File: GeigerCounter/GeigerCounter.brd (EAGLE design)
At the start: 38.1 x 35.6 mm, 37 parts, among them IC1 OPAMP-DUALU, P1 XF2M-0615-1A

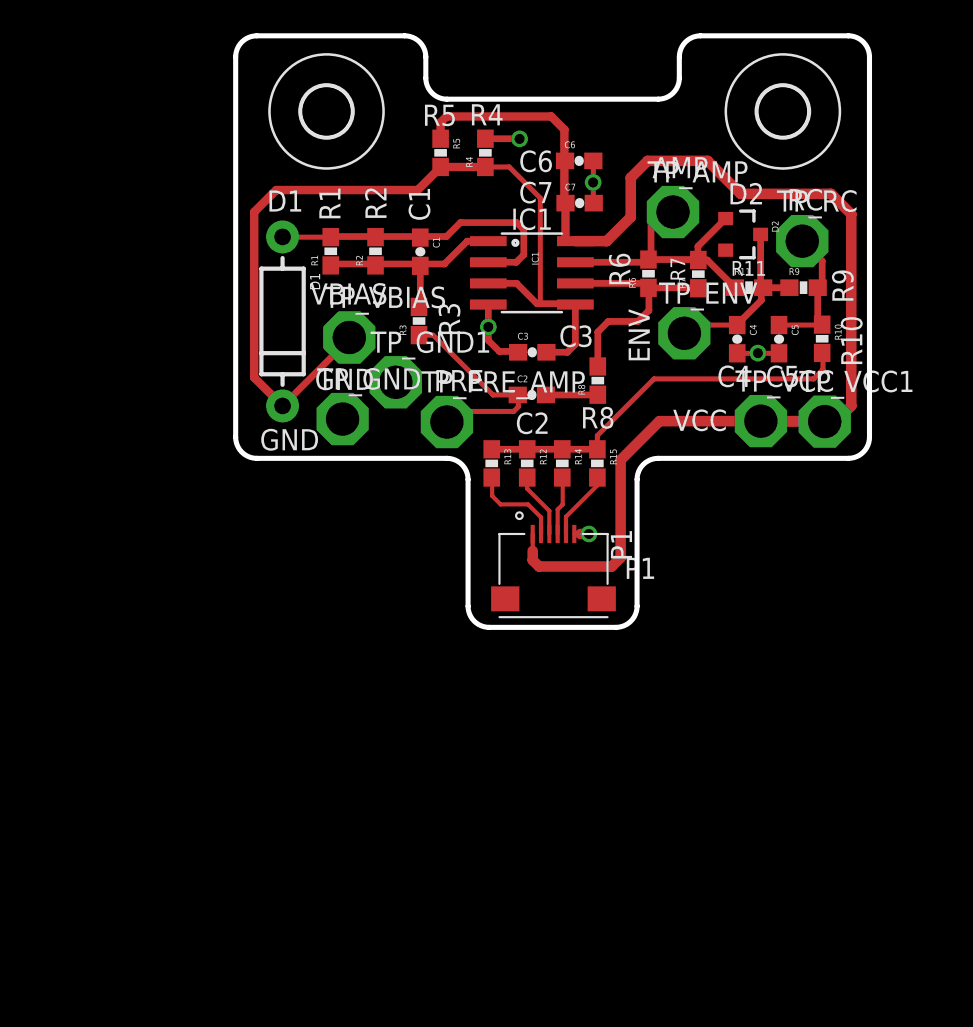
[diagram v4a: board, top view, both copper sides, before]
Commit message: All unrouted nets now routed
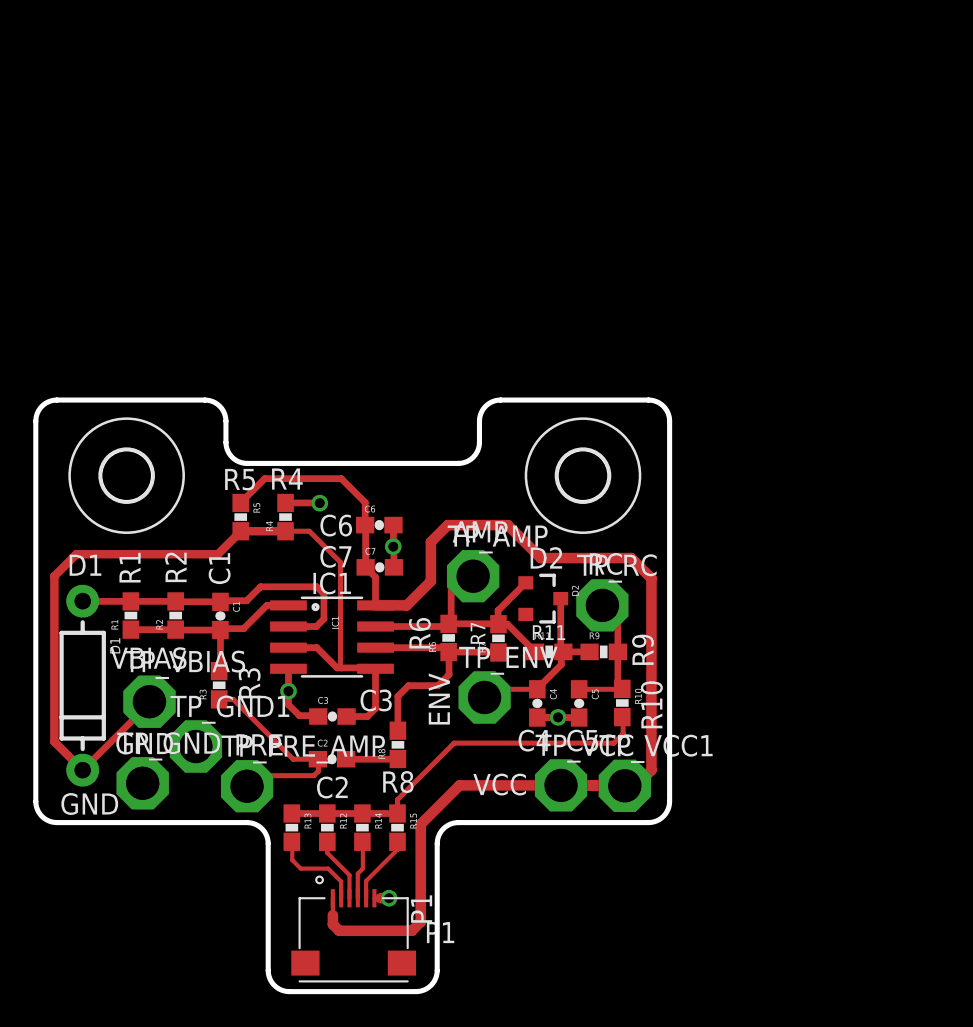
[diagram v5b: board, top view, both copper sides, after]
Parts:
- moved H2 25.0 mm to (36.1, 34.5)
- moved R14 25.0 mm to (22.9, 13.4)
- moved R8 25.0 mm to (25.0, 18.3)
- moved C1 25.0 mm to (14.3, 26.1)
- moved C4 25.0 mm to (33.4, 20.8)
- moved C5 25.0 mm to (35.9, 20.8)
- moved C7 25.0 mm to (23.9, 29.0)
- moved D2 25.0 mm to (33.7, 27.1)
- moved H1 25.0 mm to (8.69, 34.5)
- moved IC1 25.0 mm to (21.0, 24.8)
- moved P1 25.0 mm to (22.4, 6.58)
- moved R12 25.0 mm to (20.8, 13.4)
- moved R13 25.0 mm to (18.6, 13.4)
- moved R15 25.0 mm to (25.0, 13.4)
- moved R2 25.0 mm to (11.6, 26.1)
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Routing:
- net GND: track 12.3 -> 13.5 mm
